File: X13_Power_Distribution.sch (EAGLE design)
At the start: 40 parts, among them Q1 310mA/60V/1.6Ω, U1 Value, U2 Value

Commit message: routed :)
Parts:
- removed BACKPLANE_GND_1, BACKPLANE_GND_2, BACKPLANE_PWR_1, BACKPLANE_PWR_2: (no value), SparkFun-Connectors:CONN_10X2
- removed BACKPLANE_SIMBUS: 2X6 FEMALE, SparkFun-Connectors:CONN_06X2PTH_FEMALE
- added 5V_POE: POE_TERMINAL, Dist_POE:POE_TERMINAL
- added BACKPLANE_LOGIC: IPL1-107-01-L-D-RE-P, Backplane_Dist_Logic_Connector:IPL1-107-01-L-D-RE-P
- added H1, H2, H3, H4: 6-32-HOLE, Mounting Holes:6-32-HOLE
- added J1: (no value), Samtec MPPT Hermaphoditic 10 pos - MPPT-10-01-01-L-RA-SD:MPPT-10-01-01-L-RA-SD
- added R8: 10k, SparkFun-Resistors:RESISTOR0603
- U1, U2: device Dist_OR_Controller:DIST_OR_DIODE -> Dist_OR_Controller:DIST_OR_DIODEDGK0008A_M
- renumbered CONVERSION_L to CONVERSION_TOP, CONVERSION_R to CONVERSION_BOTTOM
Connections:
- removed net ALERT: BRICK1_SMBUS.4, BRICK2_SMBUS.4, R6.1
- removed net N$4: BACKPLANE_SIMBUS.11, BACKPLANE_SIMBUS.9
- net +12V: now also J1.1, J1.2, J1.3, J1.4, J1.5; no longer BACKPLANE_PWR_1.1, BACKPLANE_PWR_1.10, BACKPLANE_PWR_1.11, BACKPLANE_PWR_1.12, BACKPLANE_PWR_1.13, BACKPLANE_PWR_1.14, BACKPLANE_PWR_1.15, BACKPLANE_PWR_1.16, BACKPLANE_PWR_1.17, BACKPLANE_PWR_1.18, BACKPLANE_PWR_1.19, BACKPLANE_PWR_1.2, BACKPLANE_PWR_1.20, BACKPLANE_PWR_1.3, BACKPLANE_PWR_1.4, BACKPLANE_PWR_1.5, BACKPLANE_PWR_1.6, BACKPLANE_PWR_1.7, BACKPLANE_PWR_1.8, BACKPLANE_PWR_1.9, BACKPLANE_PWR_2.1, BACKPLANE_PWR_2.10, BACKPLANE_PWR_2.11, BACKPLANE_PWR_2.12, BACKPLANE_PWR_2.13, BACKPLANE_PWR_2.14, BACKPLANE_PWR_2.15, BACKPLANE_PWR_2.16, BACKPLANE_PWR_2.17, BACKPLANE_PWR_2.18, BACKPLANE_PWR_2.19, BACKPLANE_PWR_2.2, BACKPLANE_PWR_2.20, BACKPLANE_PWR_2.3, BACKPLANE_PWR_2.4, BACKPLANE_PWR_2.5, BACKPLANE_PWR_2.6, BACKPLANE_PWR_2.7, BACKPLANE_PWR_2.8, BACKPLANE_PWR_2.9
- net +3.3V: now also BACKPLANE_LOGIC.4, R8.2; no longer BACKPLANE_SIMBUS.7
- net +5V: now also 5V_POE.1, BACKPLANE_LOGIC.1, BACKPLANE_LOGIC.2, BACKPLANE_LOGIC.3; no longer BACKPLANE_SIMBUS.1, BACKPLANE_SIMBUS.3, BACKPLANE_SIMBUS.5
- net 12V_GND: now also J1.10, J1.6, J1.7, J1.8, J1.9; no longer BACKPLANE_GND_1.1, BACKPLANE_GND_1.10, BACKPLANE_GND_1.11, BACKPLANE_GND_1.12, BACKPLANE_GND_1.13, BACKPLANE_GND_1.14, BACKPLANE_GND_1.15, BACKPLANE_GND_1.16, BACKPLANE_GND_1.17, BACKPLANE_GND_1.18, BACKPLANE_GND_1.19, BACKPLANE_GND_1.2, BACKPLANE_GND_1.20, BACKPLANE_GND_1.3, BACKPLANE_GND_1.4, BACKPLANE_GND_1.5, BACKPLANE_GND_1.6, BACKPLANE_GND_1.7, BACKPLANE_GND_1.8, BACKPLANE_GND_1.9, BACKPLANE_GND_2.1, BACKPLANE_GND_2.10, BACKPLANE_GND_2.11, BACKPLANE_GND_2.12, BACKPLANE_GND_2.13, BACKPLANE_GND_2.14, BACKPLANE_GND_2.15, BACKPLANE_GND_2.16, BACKPLANE_GND_2.17, BACKPLANE_GND_2.18, BACKPLANE_GND_2.19, BACKPLANE_GND_2.2, BACKPLANE_GND_2.20, BACKPLANE_GND_2.3, BACKPLANE_GND_2.4, BACKPLANE_GND_2.5, BACKPLANE_GND_2.6, BACKPLANE_GND_2.7, BACKPLANE_GND_2.8, BACKPLANE_GND_2.9
- net 5V_GND: now also 5V_POE.2, BACKPLANE_LOGIC.5, BACKPLANE_LOGIC.6
- net ALERT_1: now also BACKPLANE_LOGIC.11, BRICK1_SMBUS.4, R8.1; no longer BACKPLANE_SIMBUS.4
- net ALERT_2: now also BACKPLANE_LOGIC.10, BRICK2_SMBUS.4, R6.1; no longer BACKPLANE_SIMBUS.6
- net C2_1: now also BACKPLANE_LOGIC.8; no longer BACKPLANE_SIMBUS.10
- net C2_2: now also BACKPLANE_LOGIC.7; no longer BACKPLANE_SIMBUS.12
- net CLK: now also BACKPLANE_LOGIC.9; no longer BACKPLANE_SIMBUS.8
- net DATA: now also BACKPLANE_LOGIC.12; no longer BACKPLANE_SIMBUS.2

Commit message: Routed with custom connectors
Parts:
- removed BRICK1_SMBUS, BRICK2_SMBUS: (no value), SparkFun-Connectors:CONN_05
- removed BRICK1_VIN(+), BRICK1_VIN(-), BRICK2_VIN(+), BRICK2_VIN(-): (no value), SparkFun-Connectors:CONN_05X2PTH
- removed BRICK1_VOUT(+), BRICK1_VOUT(-), BRICK2_VOUT(+), BRICK2_VOUT(-): (no value), SparkFun-Connectors:CONN_08X2
- removed CONVERSION_BOTTOM: (no value), SparkFun-Connectors:CONN_04X2
- removed CONVERSION_TOP: (no value), SparkFun-Connectors:CONN_04
- removed J1: (no value), Samtec MPPT Hermaphoditic 10 pos - MPPT-10-01-01-L-RA-SD:MPPT-10-01-01-L-RA-SD
- removed U1, U2: Value, Dist_OR_Controller:DIST_OR_DIODEDGK0008A_M
- added BACKPLANE_PWR: (no value), Samtec MPPT Hermaphoditic 10 pos - MPPT-10-01-01-L-RA-SD:MPPT-10-01-01-L-RA-SD
- added CONVERSION: DIST2CON, Dist_Convert_Connector:DIST2CON
- added OR_CON_A, OR_CON_B: Value, Dist_OR_Controller:DIST_OR_DIODEDGK0008A_M
- added U$3, U$4: (no value), Brick_Dist_Connector:DIST2BRICK
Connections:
- net N$2 renamed ON/OFF_DRIVE
- net N$3 renamed REV_DRIVE
- removed net GND: D5.C
- removed net N$10: U$1.G, U1.GATE_DRIVE, U1.GATE_PULL_DOWN
- removed net N$13: U$2.G, U2.GATE_DRIVE, U2.GATE_PULL_DOWN
- removed net N$5: C2.1, U2.VCAPH
- removed net N$6: C2.2, U2.VCAPL
- removed net N$7: C1.2, U1.VCAPL
- removed net N$9: C1.1, U1.VCAPH
- new net OR_DRIVE_A: OR_CON_A.GATE_DRIVE, OR_CON_A.GATE_PULL_DOWN, U$1.G
- new net OR_DRIVE_B: OR_CON_B.GATE_DRIVE, OR_CON_B.GATE_PULL_DOWN, U$2.G
- new net VCAPH_A: C1.1, OR_CON_A.VCAPH
- new net VCAPH_B: C2.1, OR_CON_B.VCAPH
- new net VCAPL_A: C1.2, OR_CON_A.VCAPL
- new net VCAPL_B: C2.2, OR_CON_B.VCAPL
- net +12V: now also BACKPLANE_PWR.1, BACKPLANE_PWR.2, BACKPLANE_PWR.3, BACKPLANE_PWR.4, BACKPLANE_PWR.5, OR_CON_A.CATHODE, OR_CON_B.CATHODE; no longer J1.1, J1.2, J1.3, J1.4, J1.5, U1.CATHODE, U2.CATHODE
- net +12V_A: now also OR_CON_A.ANODE, U$3.VOUT+; no longer BRICK1_VOUT(+).1, BRICK1_VOUT(+).10, BRICK1_VOUT(+).11, BRICK1_VOUT(+).12, BRICK1_VOUT(+).13, BRICK1_VOUT(+).14, BRICK1_VOUT(+).15, BRICK1_VOUT(+).16, BRICK1_VOUT(+).2, BRICK1_VOUT(+).3, BRICK1_VOUT(+).4, BRICK1_VOUT(+).5, BRICK1_VOUT(+).6, BRICK1_VOUT(+).7, BRICK1_VOUT(+).8, BRICK1_VOUT(+).9, U1.ANODE
- net +12V_B: now also OR_CON_B.ANODE, U$4.VOUT+; no longer BRICK2_VOUT(+).1, BRICK2_VOUT(+).10, BRICK2_VOUT(+).11, BRICK2_VOUT(+).12, BRICK2_VOUT(+).13, BRICK2_VOUT(+).14, BRICK2_VOUT(+).15, BRICK2_VOUT(+).16, BRICK2_VOUT(+).2, BRICK2_VOUT(+).3, BRICK2_VOUT(+).4, BRICK2_VOUT(+).5, BRICK2_VOUT(+).6, BRICK2_VOUT(+).7, BRICK2_VOUT(+).8, BRICK2_VOUT(+).9, U2.ANODE
- net +3.3V: now also CONVERSION.VOUT+_3; no longer CONVERSION_BOTTOM.3
- net +48V: now also CONVERSION.VIN+, U$3.VIN+, U$4.VIN+; no longer BRICK1_VIN(+).1, BRICK1_VIN(+).10, BRICK1_VIN(+).2, BRICK1_VIN(+).3, BRICK1_VIN(+).4, BRICK1_VIN(+).5, BRICK1_VIN(+).6, BRICK1_VIN(+).7, BRICK1_VIN(+).8, BRICK1_VIN(+).9, BRICK2_VIN(+).1, BRICK2_VIN(+).10, BRICK2_VIN(+).2, BRICK2_VIN(+).3, BRICK2_VIN(+).4, BRICK2_VIN(+).5, BRICK2_VIN(+).6, BRICK2_VIN(+).7, BRICK2_VIN(+).8, BRICK2_VIN(+).9, CONVERSION_TOP.3, CONVERSION_TOP.4
- net +5V: now also CONVERSION.VOUT+_5; no longer CONVERSION_BOTTOM.1, CONVERSION_BOTTOM.2, CONVERSION_BOTTOM.4
- net 12V_GND: now also BACKPLANE_PWR.10, BACKPLANE_PWR.6, BACKPLANE_PWR.7, BACKPLANE_PWR.8, BACKPLANE_PWR.9, D5.C, U$3.VOUT-, U$4.VOUT-; no longer BRICK1_VOUT(-).1, BRICK1_VOUT(-).10, BRICK1_VOUT(-).11, BRICK1_VOUT(-).12, BRICK1_VOUT(-).13, BRICK1_VOUT(-).14, BRICK1_VOUT(-).15, BRICK1_VOUT(-).16, BRICK1_VOUT(-).2, BRICK1_VOUT(-).3, BRICK1_VOUT(-).4, BRICK1_VOUT(-).5, BRICK1_VOUT(-).6, BRICK1_VOUT(-).7, BRICK1_VOUT(-).8, BRICK1_VOUT(-).9, BRICK2_VOUT(-).1, BRICK2_VOUT(-).10, BRICK2_VOUT(-).11, BRICK2_VOUT(-).12, BRICK2_VOUT(-).13, BRICK2_VOUT(-).14, BRICK2_VOUT(-).15, BRICK2_VOUT(-).16, BRICK2_VOUT(-).2, BRICK2_VOUT(-).3, BRICK2_VOUT(-).4, BRICK2_VOUT(-).5, BRICK2_VOUT(-).6, BRICK2_VOUT(-).7, BRICK2_VOUT(-).8, BRICK2_VOUT(-).9, J1.10, J1.6, J1.7, J1.8, J1.9
- net 48V_GND: now also CONVERSION.VIN-, U$3.VIN-, U$4.VIN-; no longer BRICK1_VIN(-).1, BRICK1_VIN(-).10, BRICK1_VIN(-).2, BRICK1_VIN(-).3, BRICK1_VIN(-).4, BRICK1_VIN(-).5, BRICK1_VIN(-).6, BRICK1_VIN(-).7, BRICK1_VIN(-).8, BRICK1_VIN(-).9, BRICK2_VIN(-).1, BRICK2_VIN(-).10, BRICK2_VIN(-).2, BRICK2_VIN(-).3, BRICK2_VIN(-).4, BRICK2_VIN(-).5, BRICK2_VIN(-).6, BRICK2_VIN(-).7, BRICK2_VIN(-).8, BRICK2_VIN(-).9, CONVERSION_TOP.1, CONVERSION_TOP.2
- net 5V_GND: now also CONVERSION.VOUT-; no longer CONVERSION_BOTTOM.5, CONVERSION_BOTTOM.6, CONVERSION_BOTTOM.7, CONVERSION_BOTTOM.8
- net ALERT_1: now also U$3.ALERT; no longer BRICK1_SMBUS.4
- net ALERT_2: now also U$4.ALERT; no longer BRICK2_SMBUS.4
- net C2_1: now also U$3.C2; no longer BRICK1_SMBUS.1
- net C2_2: now also U$4.C2; no longer BRICK2_SMBUS.1
- net CLK: now also U$3.CLK, U$4.CLK; no longer BRICK1_SMBUS.3, BRICK2_SMBUS.3
- net DATA: now also U$3.DATA, U$4.DATA; no longer BRICK1_SMBUS.5, BRICK2_SMBUS.5
- net ON/OFF: now also U$3.ON/OFF, U$4.ON/OFF; no longer BRICK1_SMBUS.2, BRICK2_SMBUS.2
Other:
- note added: "BRICK1"
- note added: "BRICK2"
- note added: "OR CONTROLLERS"
- note removed: "PULL-UP RESISTORS"
- moved on the sheet: BACKPLANE_LOGIC, C1, C2, C3, D5, R4, R5, R6, R7, R8, U$1, U$2

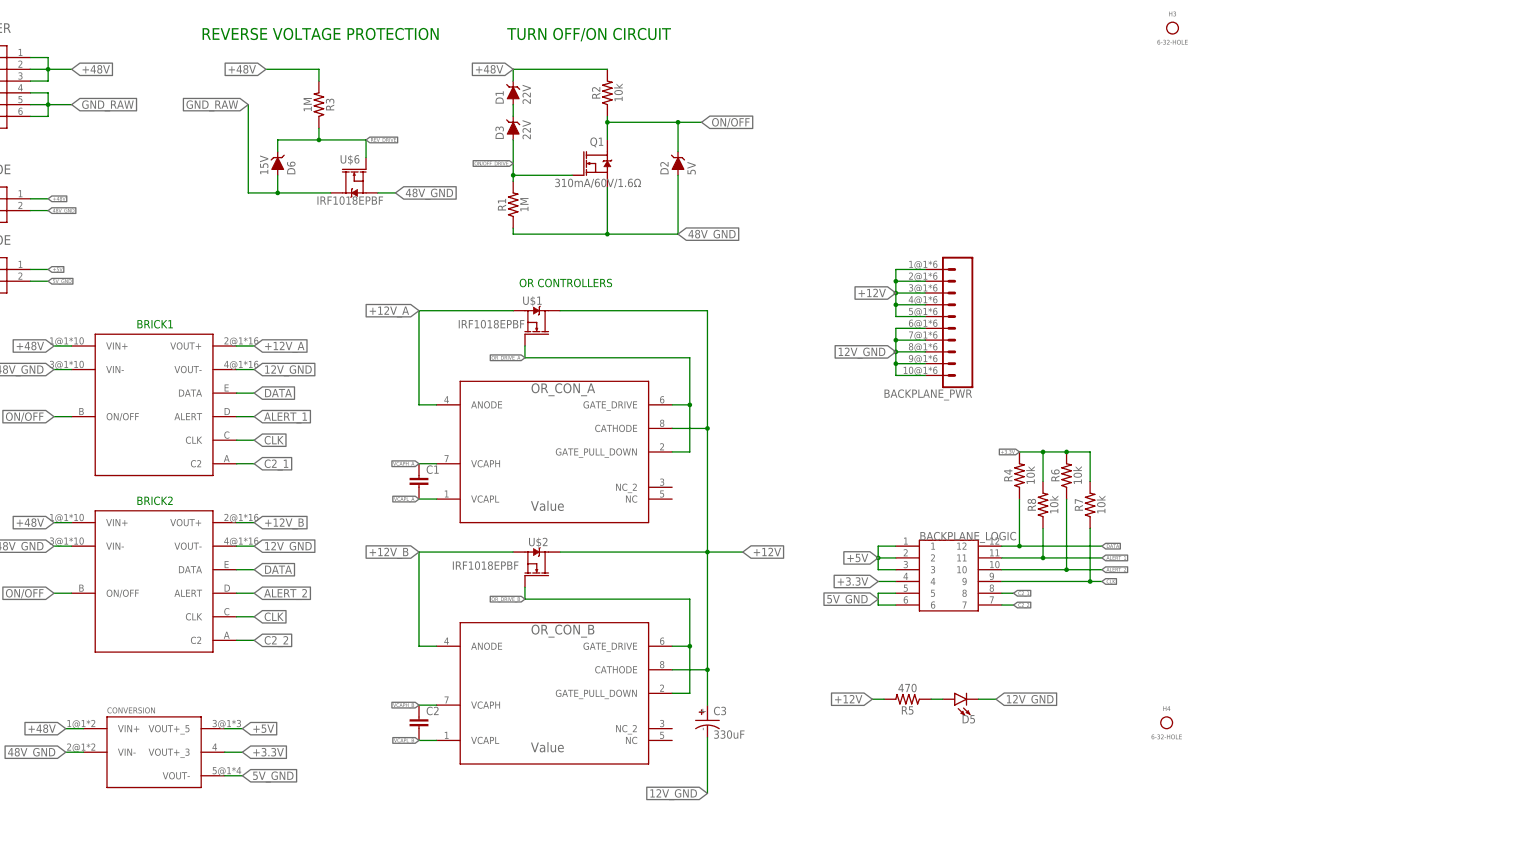
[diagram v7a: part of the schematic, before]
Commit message: Exports and cleaning up git for ordering
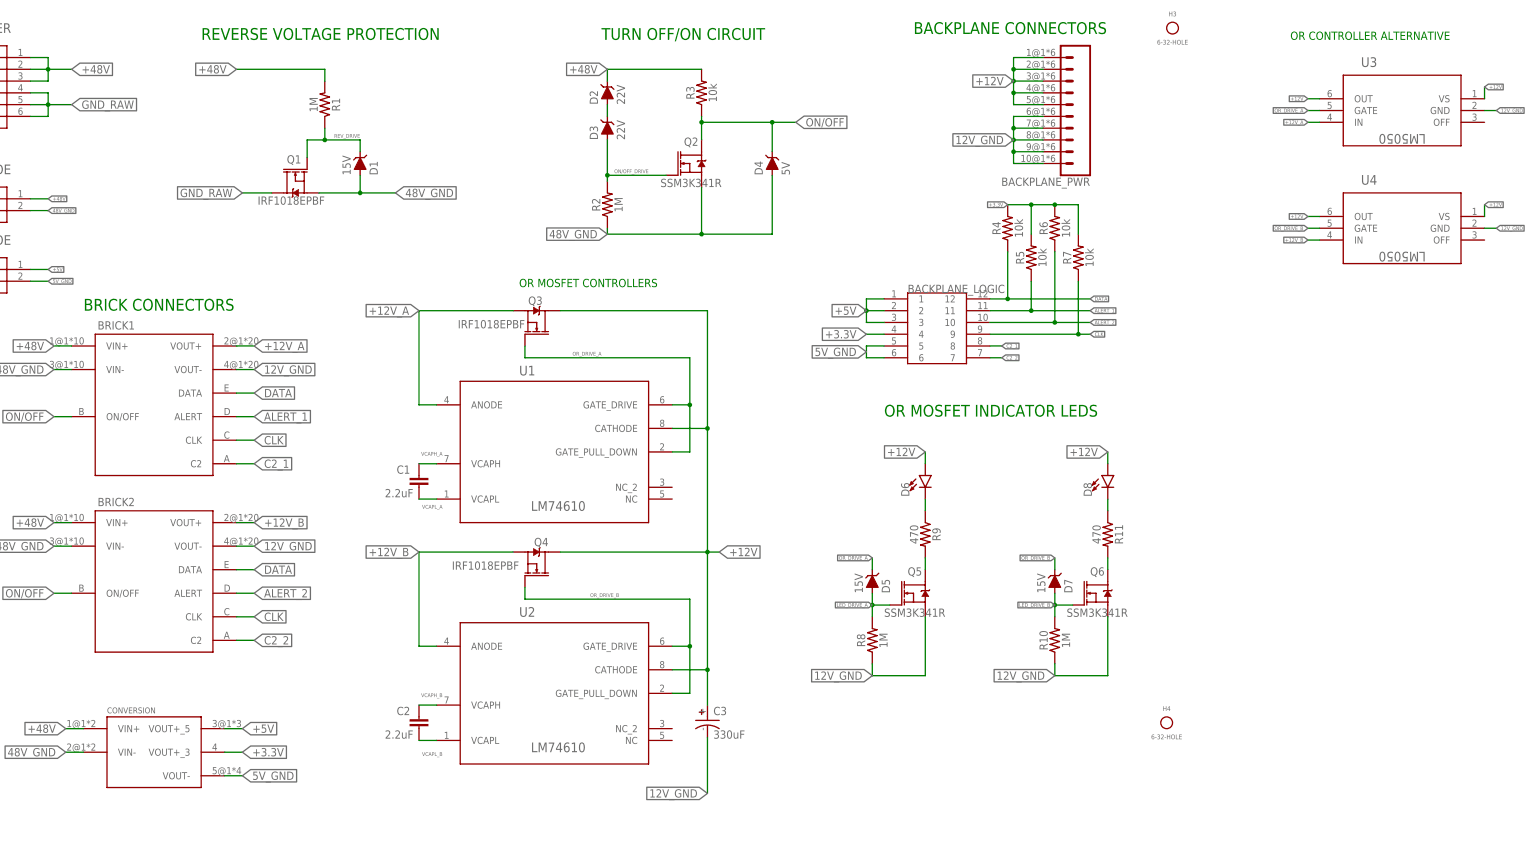
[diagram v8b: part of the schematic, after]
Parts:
- removed U$3, U$4: (no value), Brick_Dist_Connector:DIST2BRICK
- removed U$6: IRF1018EPBF, Reverse_Voltage_NMOS:IRF1018EPBF
- added BRICK1, BRICK2: DIST2BRICKVER_D2, Brick_Dist_Connector:DIST2BRICKVER_D2
- added D4: 5V, SparkFun-DiscreteSemi:DIODE-ZENER-BZT52C3V6S
- added D7: 15V, SparkFun-DiscreteSemi:DIODE-ZENER-BZT52C3V6S
- added D8: (no value), SparkFun-LED:LED0603
- added Q2, Q5, Q6: SSM3K341R, SparkFun-DiscreteSemi:MOSFET-NCH-2N7002PW
- added R10: 1M, SparkFun-Resistors:RESISTOR0603
- added R11, R9: 470, SparkFun-Resistors:RESISTOR0603
- added U3, U4: LM5050, Dist_OR_Controller:DIST_OR_CONTROL_ALTMK06A-M
- BACKPLANE_LOGIC: value IPL1-107-01-L-D-RE-P -> IPL1-106-01-L-D-K; device Backplane_Dist_Logic_Connector:IPL1-107-01-L-D-RE-P -> Backplane_Dist_Logic_Connector:IPL1-106-01-L-D-K
- C1, C2: value 0.1UF-0603-100V-10% -> 2.2uF
- D1: value 22V -> 15V
- D2: value 5V -> 22V
- D5: value (none) -> 15V; device SparkFun-LED:LED0603 -> SparkFun-DiscreteSemi:DIODE-ZENER-BZT52C3V6S
- D6: value 15V -> (none); device SparkFun-DiscreteSemi:DIODE-ZENER-BZT52C3V6S -> SparkFun-LED:LED0603
- Q1: value 310mA/60V/1.6Ω -> IRF1018EPBF; device SparkFun-DiscreteSemi:MOSFET-NCH-2N7002PW -> Reverse_Voltage_NMOS:IRF1018EPBF
- R1: SPICEPREFIX R -> (none)
- R2: value 10k -> 1M
- R3: value 1M -> 10k; SPICEPREFIX (none) -> R
- R5: value 470 -> 10k
- R8: value 10k -> 1M; SPICEPREFIX (none) -> R
- U1, U2: value Value -> LM74610
- renumbered OR_CON_A to U1, OR_CON_B to U2, U$1 to Q3, U$2 to Q4
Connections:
- removed net N$8: D5.A, R5.1
- new net LED_DRIVE_A: D5.A, Q5.G, R8.2
- new net LED_DRIVE_B: D7.A, Q6.G, R10.2
- new net N$4: Q5.D, R9.2
- new net N$5: D6.C, R9.1
- new net N$6: Q6.D, R11.2
- new net N$7: D8.C, R11.1
- net +12V: now also D6.A, D8.A, U3.OUT, U3.VS, U4.OUT, U4.VS; no longer R5.2
- net +12V_A: now also BRICK1.VOUT+, U3.IN; no longer U$3.VOUT+
- net +12V_B: now also BRICK2.VOUT+, U4.IN; no longer U$4.VOUT+
- net +3.3V: now also R5.2; no longer R8.2
- net +48V: now also BRICK1.VIN+, BRICK2.VIN+, D2.C, R1.2; no longer D1.C, R2.2, U$3.VIN+, U$4.VIN+
- net 12V_GND: now also BRICK1.VOUT-, BRICK2.VOUT-, Q5.S, Q6.S, R10.1, R8.1, U3.GND, U4.GND; no longer D5.C, U$3.VOUT-, U$4.VOUT-
- net 48V_GND: now also BRICK1.VIN-, BRICK2.VIN-, D1.A, D4.A, Q2.S, R2.1; no longer D2.A, R1.1, U$3.VIN-, U$4.VIN-, U$6.S
- net ALERT_1: now also BRICK1.ALERT, R5.1; no longer R8.1, U$3.ALERT
- net ALERT_2: now also BRICK2.ALERT; no longer U$4.ALERT
- net C2_1: now also BRICK1.C2; no longer U$3.C2
- net C2_2: now also BRICK2.C2; no longer U$4.C2
- net CLK: now also BRICK1.CLK, BRICK2.CLK; no longer U$3.CLK, U$4.CLK
- net DATA: now also BRICK1.DATA, BRICK2.DATA; no longer U$3.DATA, U$4.DATA
- net GND_RAW: now also Q1.D; no longer D6.A, U$6.D
- net N$1: now also D2.A; no longer D1.A
- net ON/OFF: now also BRICK1.ON/OFF, BRICK2.ON/OFF, D4.C, Q2.D, R3.1; no longer D2.C, Q1.D, R2.1, U$3.ON/OFF, U$4.ON/OFF
- net ON/OFF_DRIVE: now also Q2.G, R2.2; no longer Q1.G, R1.2
- net OR_DRIVE_A: now also D5.C, U3.GATE
- net OR_DRIVE_B: now also D7.C, U4.GATE
- net REV_DRIVE: now also D1.C, Q1.G, R1.1; no longer D6.C, R3.1, U$6.G
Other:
- note added: "BACKPLANE CONNECTORS"
- note added: "BRICK CONNECTORS"
- note added: "OR CONTROLLER ALTERNATIVE"
- note added: "OR MOSFET CONTROLLERS"
- note added: "OR MOSFET INDICATOR LEDS"
- note removed: "BRICK1"
- note removed: "BRICK2"
- note removed: "OR CONTROLLERS"
- moved on the sheet: BACKPLANE_LOGIC, BACKPLANE_PWR, D1, D2, D3, R1, R2, R3, R4, R5, R6, R7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
